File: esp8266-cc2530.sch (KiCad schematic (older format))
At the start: 26 parts

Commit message: created cc2592 part, added to schematic undecided if RF frontend should be RFX2401 or CC2592
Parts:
- added C? (x3): 1u, symbol Device:C
- added C?: 1.8p, symbol Device:C
- added C?: 2.2p, symbol Device:C
- added C?: 1p, symbol Device:C
- added C?: 18p, symbol Device:C
- added L?: 15n, symbol Device:L
- added L?: 1n, symbol Device:L
- added L?: 3n, symbol Device:L
- added R?: 3.9k, symbol Device:R
- added R? (x3): 1k, symbol Device:R
- added U?: CC2592, symbol projectLib:CC2592
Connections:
- net labels added: P0_7, P1_0, P1_1
- wire segments 101 -> 129

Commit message: schematic updates * updated TODO * added bypass to RF2401
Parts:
- added C?: DNP, symbol Device:C
- added R?: DNP, symbol Device:R
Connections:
- wire segments 129 -> 135
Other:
- note added: "TODO\n* Figure out TX/RX En pinout\n* add cc2530 programming header\n* cc2530 regulator?"
- note removed: "TODO\n* Figure out TX/RX En pinout"
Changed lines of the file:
@@
 U 1 1 5EA117C8
 P 1900 3100
-F 0 "U?" H 1900 2211 50  0000 C CNN
-F 1 "WeMos_D1_mini" H 1900 2120 50  0000 C CNN
+F 0 "U?" H 1600 3900 50  0000 C CNN
+F 1 "WeMos_D1_mini" H 1400 2300 50  0000 C CNN
 F 2 "Module:WEMOS_D1_mini_light" H 1900 1950 50  0001 C CNN
 F 3 "https://wiki.wemos.cc/products:d1:d1_mini#documentation" H 50  1950 50  0001 C CNN
@@
 Wire Wire Line
 	8000 3200 7900 3200
-Wire Wire Line
-	8150 3050 8000 3050
 Connection ~ 8000 3050
 Wire Wire Line
@@
 Connection ~ 9800 2450
 Text Notes 8500 950  0    50   ~ 0
-TODO\n* Figure out TX/RX En pinout
+TODO\n* Figure out TX/RX En pinout\n* add cc2530 programming header\n* cc2530 regulator?
 $Comp
 L Device:C C?
@@
 U 1 1 5EACFB8A
 P 8600 5950
-F 0 "U?" H 9094 6396 50  0000 L CNN
-F 1 "CC2592" H 9094 6305 50  0000 L CNN
+F 0 "U?" H 9000 7000 50  0000 L CNN
+F 1 "CC2592" H 8550 6300 50  0000 L CNN
 F 2 "" H 8600 5950 50  0001 C CNN
 F 3 "" H 8600 5950 50  0001 C CNN
@@
 Text Label 7250 6000 2    50   ~ 0
 P1_1
+$Comp
+L Device:C C?
+U 1 1 5EB635D2
+P 8200 1600
+F 0 "C?" V 7948 1600 50  0000 C CNN
+F 1 "DNP" V 8039 1600 50  0000 C CNN
+F 2 "" H 8238 1450 50  0001 C CNN
+F 3 "~" H 8200 1600 50  0001 C CNN
+	1    8200 1600
+	0    -1   1    0
+$EndComp
+$Comp
+L Device:R R?
+U 1 1 5EB77ED4
+P 9750 1600
+F 0 "R?" H 9680 1554 50  0000 R CNN
+F 1 "DNP" H 9680 1645 50  0000 R CNN
+F 2 "" V 9680 1600 50  0001 C CNN
+F 3 "~" H 9750 1600 50  0001 C CNN
+	1    9750 1600
+	0    1    1    0
+$EndComp
+Wire Wire Line
+	9900 3050 10300 3050
+Text Label 8250 3350 2    50   ~ 0
+P1_1
+Text Label 8250 3650 2    50   ~ 0
+P1_0
+Wire Wire Line
+	9900 1600 10300 1600
+Wire Wire Line
+	8350 1600 9600 1600
+Wire Wire Line
+	8000 3050 8050 3050
+Wire Wire Line
+	10300 1600 10300 3050
+Wire Wire Line
+	8050 1600 8050 3050
+Connection ~ 8050 3050
+Wire Wire Line
+	8050 3050 8150 3050
+$Comp
+L power:GND #PWR?
+U 1 1 5EBADD70
+P 1900 3900
+F 0 "#PWR?" H 1900 3650 50  0001 C CNN
+F 1 "GND" H 1905 3727 50  0000 C CNN
+F 2 "" H 1900 3900 50  0001 C CNN
+F 3 "" H 1900 3900 50  0001 C CNN
+	1    1900 3900
+	1    0    0    -1
+$EndComp
+Text Label 2300 3000 0    50   ~ 0
+ESP_RX
+Text Label 2300 3100 0    50   ~ 0
+ESP_TX
 $EndSCHEMATC

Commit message: add cc2530 programming header
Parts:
- added C?: 1u, symbol Device:C
- added J?: CC2530_programmingHeader, symbol projectLib:CC2530_programmingHeader
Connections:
- net labels added: P2_1, P2_2, ~RST
- wire segments 135 -> 140
- no-connect marks 0 -> 5
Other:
- note added: "TODO\n* cc2530 regulator?"
- note removed: "TODO\n* Figure out TX/RX En pinout\n* add cc2530 programming header\n* cc2530 regulator?"
- moved on the sheet: C?, Y?

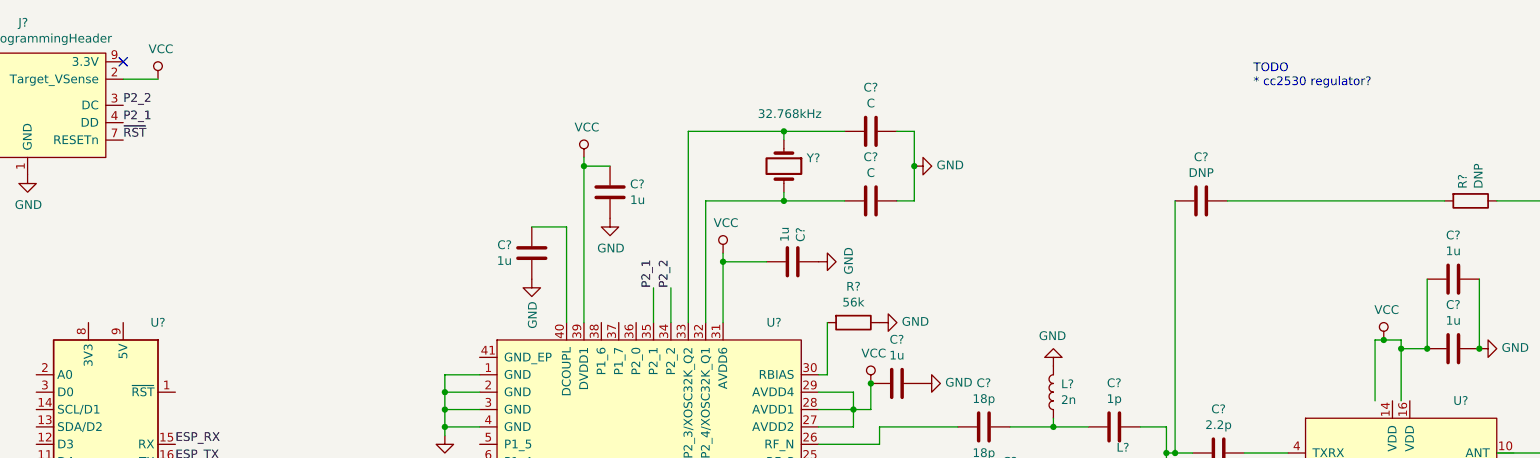
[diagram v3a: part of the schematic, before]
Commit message: added regulator for cc2530
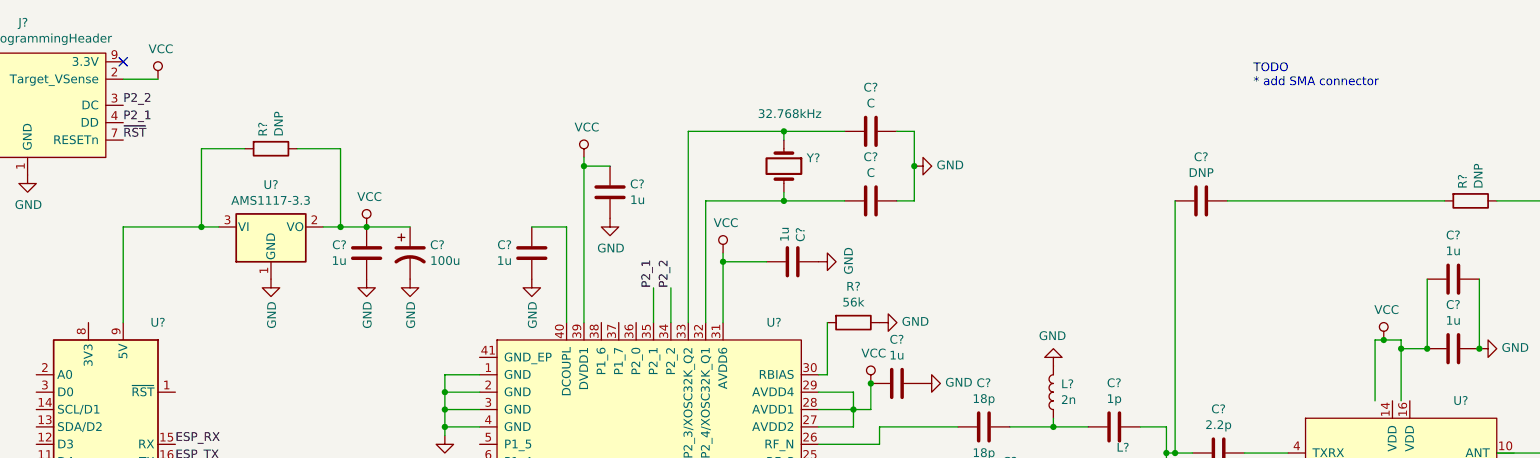
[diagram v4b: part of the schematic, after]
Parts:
- added C?: 1u, symbol Device:C
- added C?: 100u, symbol Device:CP1
- added R?: DNP, symbol Device:R
- added U?: AMS1117-3.3, Package_TO_SOT_SMD:SOT-223-3_TabPin2, symbol Regulator_Linear:AMS1117-3.3
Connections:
- wire segments 140 -> 150
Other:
- note added: "TODO\n* add SMA connector"
- note removed: "TODO\n* cc2530 regulator?"
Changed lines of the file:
@@
 Connection ~ 9800 2450
 Text Notes 8500 950  0    50   ~ 0
-TODO\n* cc2530 regulator?
+TODO\n* add SMA connector
 $Comp
 L Device:C C?
@@
 	1    0    0    -1
 $EndComp
+$Comp
+L Regulator_Linear:AMS1117-3.3 U?
+U 1 1 5EC2B8A4
+P 2850 1750
+F 0 "U?" H 2850 1992 50  0000 C CNN
+F 1 "AMS1117-3.3" H 2850 1901 50  0000 C CNN
+F 2 "Package_TO_SOT_SMD:SOT-223-3_TabPin2" H 2850 1950 50  0001 C CNN
+F 3 "http://www.advanced-monolithic.com/pdf/ds1117.pdf" H 2950 1500 50  0001 C CNN
+	1    2850 1750
+	1    0    0    -1
+$EndComp
+$Comp
+L Device:R R?
+U 1 1 5EC30553
+P 2850 1300
+F 0 "R?" H 2780 1254 50  0000 R CNN
+F 1 "DNP" H 2780 1345 50  0000 R CNN
+F 2 "" V 2780 1300 50  0001 C CNN
+F 3 "~" H 2850 1300 50  0001 C CNN
+	1    2850 1300
+	0    1    1    0
+$EndComp
+$Comp
+L Device:C C?
+U 1 1 5EC30A4C
+P 3400 1900
+F 0 "C?" H 3286 1854 50  0000 R CNN
+F 1 "1u" H 3286 1945 50  0000 R CNN
+F 2 "" H 3438 1750 50  0001 C CNN
+F 3 "~" H 3400 1900 50  0001 C CNN
+	1    3400 1900
+	1    0    0    1
+$EndComp
+$Comp
+L Device:CP1 C?
+U 1 1 5EC31ECE
+P 3650 1900
+F 0 "C?" H 3765 1946 50  0000 L CNN
+F 1 "100u" H 3765 1855 50  0000 L CNN
+F 2 "" H 3650 1900 50  0001 C CNN
+F 3 "~" H 3650 1900 50  0001 C CNN
+	1    3650 1900
+	1    0    0    -1
+$EndComp
+$Comp
+L power:GND #PWR?
+U 1 1 5EC3261B
+P 2850 2050
+F 0 "#PWR?" H 2850 1800 50  0001 C CNN
+F 1 "GND" V 2855 1922 50  0000 R CNN
+F 2 "" H 2850 2050 50  0001 C CNN
+F 3 "" H 2850 2050 50  0001 C CNN
+	1    2850 2050
+	1    0    0    -1
+$EndComp
+$Comp
+L power:GND #PWR?
+U 1 1 5EC32AB8
+P 3650 2050
+F 0 "#PWR?" H 3650 1800 50  0001 C CNN
+F 1 "GND" V 3655 1922 50  0000 R CNN
+F 2 "" H 3650 2050 50  0001 C CNN
+F 3 "" H 3650 2050 50  0001 C CNN
+	1    3650 2050
+	1    0    0    -1
+$EndComp
+$Comp
+L power:GND #PWR?
+U 1 1 5EC32D7E
+P 3400 2050
+F 0 "#PWR?" H 3400 1800 50  0001 C CNN
+F 1 "GND" V 3405 1922 50  0000 R CNN
+F 2 "" H 3400 2050 50  0001 C CNN
+F 3 "" H 3400 2050 50  0001 C CNN
+	1    3400 2050
+	1    0    0    -1
+$EndComp
+Wire Wire Line
+	3150 1750 3250 1750
+Connection ~ 3400 1750
+Wire Wire Line
+	3400 1750 3650 1750
+$Comp
+L power:VCC #PWR?
+U 1 1 5EC3EB30
+P 3400 1750
+F 0 "#PWR?" H 3400 1600 50  0001 C CNN
+F 1 "VCC" H 3417 1923 50  0000 C CNN
+F 2 "" H 3400 1750 50  0001 C CNN
+F 3 "" H 3400 1750 50  0001 C CNN
+	1    3400 1750
+	1    0    0    -1
+$EndComp
+Wire Wire Line
+	2550 1750 2450 1750
+Wire Wire Line
+	2000 1750 2000 2300
+Wire Wire Line
+	2700 1300 2450 1300
+Wire Wire Line
+	2450 1300 2450 1750
+Connection ~ 2450 1750
+Wire Wire Line
+	2450 1750 2000 1750
+Wire Wire Line
+	3000 1300 3250 1300
+Wire Wire Line
+	3250 1300 3250 1750
+Connection ~ 3250 1750
+Wire Wire Line
+	3250 1750 3400 1750
 $EndSCHEMATC

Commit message: remove cc2592 from schematic
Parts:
- removed C? (x3): 1u, symbol Device:C
- removed C?: 1.8p, symbol Device:C
- removed C?: 2.2p, symbol Device:C
- removed C?: 1p, symbol Device:C
- removed C?: 18p, symbol Device:C
- removed L?: 15n, symbol Device:L
- removed L?: 1n, symbol Device:L
- removed L?: 3n, symbol Device:L
- removed R?: 3.9k, symbol Device:R
- removed R? (x3): 1k, symbol Device:R
- removed U?: CC2592, symbol projectLib:CC2592
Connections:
- net labels removed: P0_7
- wire segments 150 -> 122

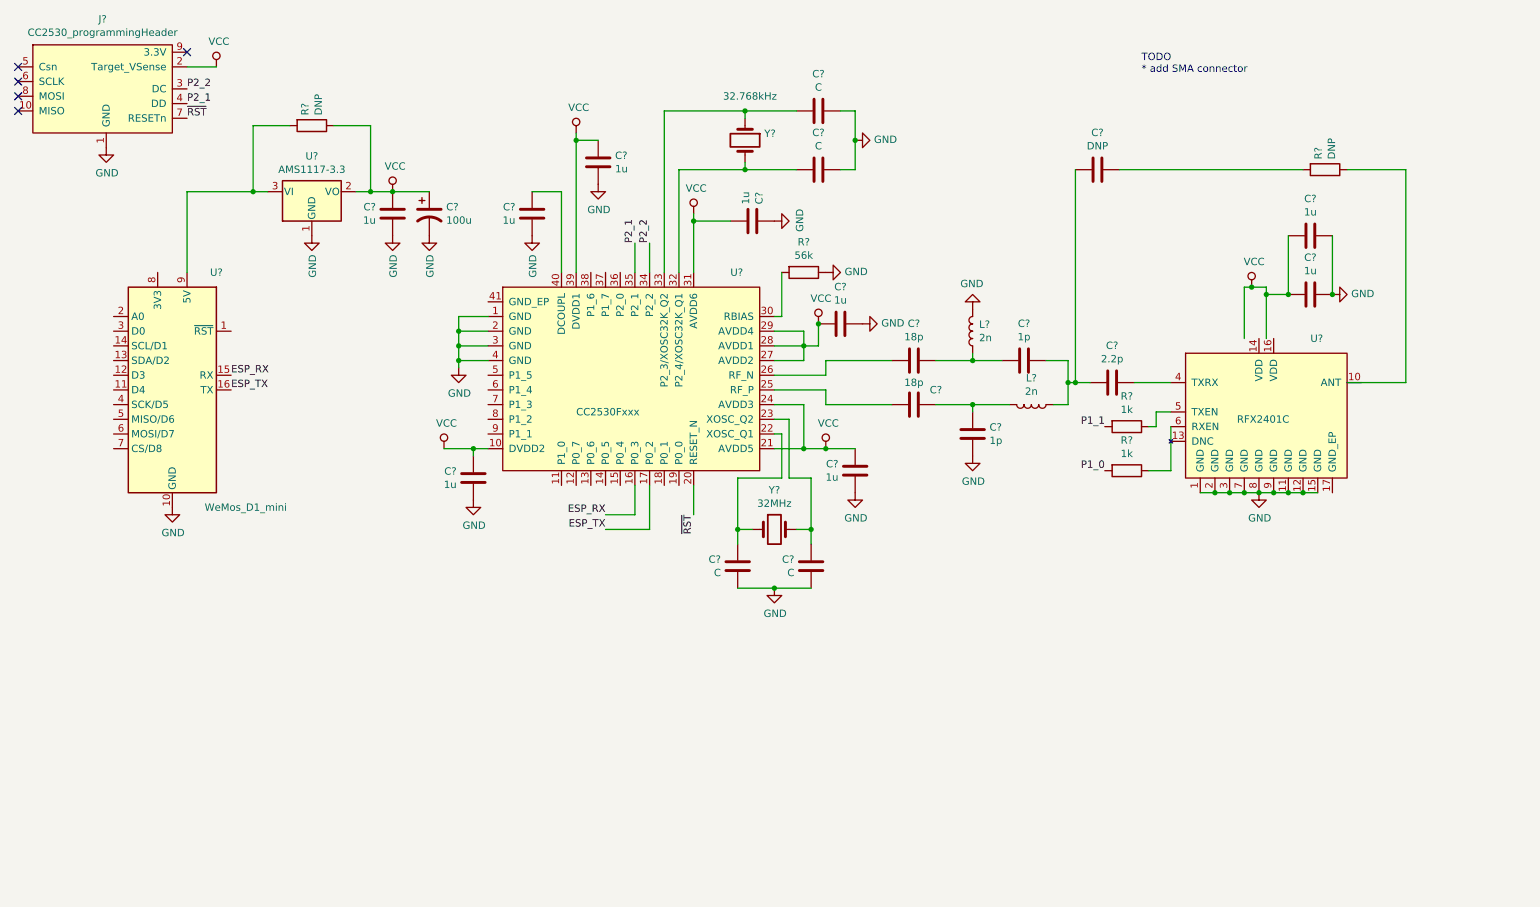
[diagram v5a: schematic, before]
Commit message: annotated schematic, fixed DRCs, needed to fork D1-mini symbol
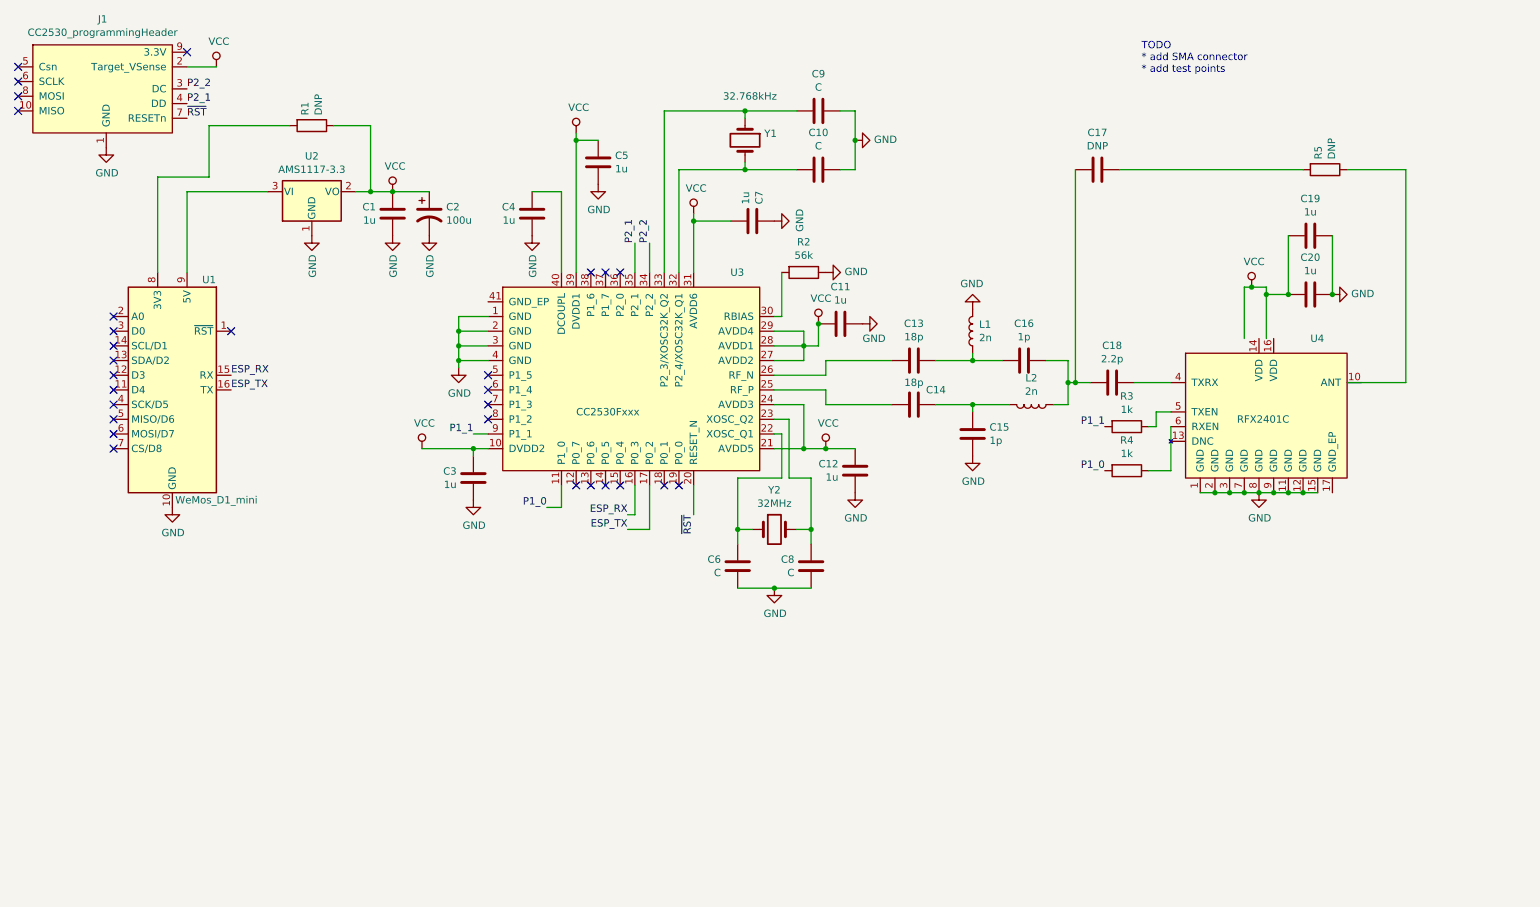
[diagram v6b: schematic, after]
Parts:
- removed U?: WeMos_D1_mini, Module:WEMOS_D1_mini_light, symbol MCU_Module:WeMos_D1_mini
- added U1: WeMos_D1_mini, Module:WEMOS_D1_mini_light, symbol projectLib:WeMos_D1_mini
- gave numbers to parts that had none: 33
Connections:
- net ESP_RX: now also U1.15 (RX)
- net ESP_TX: now also U1.16 (TX)
- net GND: now also U1.10 (GND)
- net P1_0: now also U3.11 (P1_0)
- net P1_1: now also U3.9 (P1_1)
- net at U2.3 (VI): now also U1.9 (5V); no longer R1.2
- new net: R1.2, U1.8 (3V3)
- no-connect marks 5 -> 29
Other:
- note added: "TODO\n* add SMA connector\n* add test points"
- note removed: "TODO\n* add SMA connector"

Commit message: begining to assign LCSC part numbers
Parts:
- added Y2: 32MHz, Crystal:Crystal_SMD_SeikoEpson_FA238-4Pin_3.2x2.5mm, symbol Device:Crystal_GND24
- C1, C11, C12, C19, C20, C3, C4, C5, C7: footprint (none) -> Capacitor_SMD:C_0805_2012Metric; JLCPCB Basic (none) -> Y; LCSC (none) -> C28323
- C10, C9: value C -> 27p; footprint (none) -> Capacitor_SMD:C_0805_2012Metric; JLCPCB Basic (none) -> Y; LCSC (none) -> C8031
- C13, C14: footprint (none) -> Capacitor_SMD:C_0805_2012Metric; JLCPCB Basic (none) -> Y; LCSC (none) -> C1797
- C15, C16: footprint (none) -> Capacitor_SMD:C_0805_2012Metric; JLCPCB Basic (none) -> Y; LCSC (none) -> C14971
- C17, C18: footprint (none) -> Capacitor_SMD:C_0805_2012Metric
- C2: footprint (none) -> Capacitor_Tantalum_SMD:CP_EIA-3528-21_Kemet-B; JLCPCB Basic (none) -> Y; LCSC (none) -> C16133
- C6, C8: value C -> 15p; footprint (none) -> Capacitor_SMD:C_0805_2012Metric; JLCPCB Basic (none) -> Y; LCSC (none) -> C1794
- R1, R5: footprint (none) -> Resistor_SMD:R_0805_2012Metric
- R2: footprint (none) -> Resistor_SMD:R_0805_2012Metric; JLCPCB Basic (none) -> Y; LCSC (none) -> C17756
- R3, R4: footprint (none) -> Resistor_SMD:R_0805_2012Metric; JLCPCB Basic (none) -> Y; LCSC (none) -> C17513
- U2: JLCPCB Basic (none) -> Y; LCSC (none) -> C6186
- U3: JLCPCB Basic (none) -> Y; LCSC (none) -> C9120
- U4: JLCPCB Basic (none) -> N; LCSC (none) -> C19213
- Y1: JLCPCB Basic (none) -> Y; LCSC (none) -> C32346
- Y2: footprint (none) -> Crystal:Crystal_SMD_SeikoEpson_FA238-4Pin_3.2x2.5mm; JLCPCB Basic (none) -> N; LCSC (none) -> C91742
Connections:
- net GND: now also Y2.2, Y2.4
- net at C6.2, U3.22 (XOSC_Q1): now also Y2.1; no longer Y2.1
- net at C8.2, U3.23 (XOSC_Q2): now also Y2.3; no longer Y2.2
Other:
- moved on the sheet: C6, C8, Y2
